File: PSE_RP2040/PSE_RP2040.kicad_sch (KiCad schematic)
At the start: 69 parts, among them IC2 SAM-M8Q-0, J1 USB_B, J2 USB_B_Micro, J3 8P8C_LED, Q1 DTC114Y, Q2 Q_PMOS_GSD, SW1 SW_Push, U1 RP2040, U2 PCF8563T, U6 PAM7Q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

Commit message: OR a diodi, connettore ext PoE
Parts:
- C2, C5: footprint (none) -> Capacitor_SMD:C_0603_1608Metric
- D1: value (none) -> D_Schottky
- D2, D3: footprint (none) -> Package_SO:SO-4_4.4x3.6mm_P2.54mm
- H1, H2, H3, H4: footprint (none) -> MountingHole:MountingHole_3mm
- IC2: footprint (none) -> PSE2021:SAM-M8Q
- J4: value (none) -> Conn_01x03; footprint (none) -> Connector_PinHeader_2.54mm:PinHeader_1x03_P2.54mm_Vertical
- R37: value (none) -> 1k; footprint (none) -> Resistor_SMD:R_0603_1608Metric
- SW2: value (none) -> SW_Push; footprint (none) -> Button_Switch_SMD:SW_SPST_EVQP0
- U5: value (none) -> W25Q16JVUXIQ; footprint (none) -> Package_SO:SOIC-8_5.275x5.275mm_P1.27mm
- Y2: footprint (none) -> Crystal:Crystal_SMD_3225-4Pin_3.2x2.5mm_HandSoldering
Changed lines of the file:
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@@
       (effects (font (size 1.27 1.27)) (justify left))
     )
-    (property "Footprint" "" (id 2) (at 105.1052 97.79 0)
+    (property "Footprint" "Capacitor_SMD:C_0603_1608Metric" (id 2) (at 105.1052 97.79 0)
       (effects (font (size 1.27 1.27)) hide)
     )
@@
       (effects (font (size 1.27 1.27)) (justify left))
     )
-    (property "Footprint" "" (id 2) (at 127.9652 97.79 0)
+    (property "Footprint" "Capacitor_SMD:C_0603_1608Metric" (id 2) (at 127.9652 97.79 0)
       (effects (font (size 1.27 1.27)) hide)
     )
@@
       (effects (font (size 1.27 1.27)) (justify left))
     )
-    (property "Footprint" "" (id 2) (at 375.92 148.59 0)
+    (property "Footprint" "PSE2021:SAM-M8Q" (id 2) (at 375.92 148.59 0)
       (effects (font (size 1.27 1.27)) (justify left) hide)
     )
@@
     (in_bom yes) (on_board yes)
     (property "Reference" "U5" (id 0) (at 345.44 50.419 0))
-    (property "Value" "" (id 1) (at 345.44 52.7304 0))
-    (property "Footprint" "" (id 2) (at 341.63 63.5 0)
+    (property "Value" "W25Q16JVUXIQ" (id 1) (at 345.44 52.7304 0))
+    (property "Footprint" "Package_SO:SOIC-8_5.275x5.275mm_P1.27mm" (id 2) (at 341.63 63.5 0)
       (effects (font (size 1.27 1.27)) hide)
     )
@@
       (effects (font (size 1.27 1.27)) (justify left))
     )
-    (property "Footprint" "" (id 2) (at 115.57 86.36 0)
+    (property "Footprint" "Crystal:Crystal_SMD_3225-4Pin_3.2x2.5mm_HandSoldering" (id 2) (at 115.57 86.36 0)
       (effects (font (size 1.27 1.27)) hide)
     )
@@
     (in_bom yes) (on_board yes)
     (property "Reference" "J4" (id 0) (at 274.32 95.25 0))
-    (property "Value" "" (id 1) (at 278.9428 91.8464 0))
-    (property "Footprint" "" (id 2) (at 276.86 97.79 0)
+    (property "Value" "Conn_01x03" (id 1) (at 278.9428 91.8464 0))
+    (property "Footprint" "Connector_PinHeader_2.54mm:PinHeader_1x03_P2.54mm_Vertical" (id 2) (at 276.86 97.79 0)
       (effects (font (size 1.27 1.27)) hide)
     )
@@
       (effects (font (size 1.27 1.27)) (justify left))
     )
-    (property "Value" "" (id 1) (at 115.57 40.6399 0)
-      (effects (font (size 1.27 1.27)) (justify left))
-    )
-    (property "Footprint" "" (id 2) (at 111.252 39.37 90)
+    (property "Value" "1k" (id 1) (at 115.57 40.6399 0)
+      (effects (font (size 1.27 1.27)) (justify left))
+    )
+    (property "Footprint" "Resistor_SMD:R_0603_1608Metric" (id 2) (at 111.252 39.37 90)
       (effects (font (size 1.27 1.27)) hide)
     )
@@
       (effects (font (size 1.27 1.27)) (justify right))
     )
-    (property "Value" "" (id 1) (at 53.34 122.2374 90)
+    (property "Value" "D_Schottky" (id 1) (at 53.34 122.2374 90)
       (effects (font (size 1.27 1.27)) (justify right))
     )
@@
     (property "Reference" "H1" (id 0) (at 24.13 271.3822 0))
     (property "Value" "MountingHole" (id 1) (at 24.13 273.9191 0))
-    (property "Footprint" "" (id 2) (at 24.13 276.86 0)
+    (property "Footprint" "MountingHole:MountingHole_3mm" (id 2) (at 24.13 276.86 0)
       (effects (font (size 1.27 1.27)) hide)
     )
@@
     (property "Reference" "D3" (id 0) (at 211.4558 213.3433 90))
     (property "Value" "D_Bridge_+-AA" (id 1) (at 211.4558 215.8802 90))
-    (property "Footprint" "" (id 2) (at 198.12 217.17 0)
+    (property "Footprint" "Package_SO:SO-4_4.4x3.6mm_P2.54mm" (id 2) (at 198.12 217.17 0)
       (effects (font (size 1.27 1.27)) hide)
     )
@@
       (effects (font (size 1.27 1.27)) (justify left))
     )
-    (property "Value" "" (id 1) (at 116.84 50.7999 90)
-      (effects (font (size 1.27 1.27)) (justify left))
-    )
-    (property "Footprint" "" (id 2) (at 118.11 49.53 0)
+    (property "Value" "SW_Push" (id 1) (at 116.84 50.7999 90)
+      (effects (font (size 1.27 1.27)) (justify left))
+    )
+    (property "Footprint" "Button_Switch_SMD:SW_SPST_EVQP0" (id 2) (at 118.11 49.53 0)
       (effects (font (size 1.27 1.27)) hide)
     )
@@
     (property "Reference" "D2" (id 0) (at 211.4558 189.7211 90))
     (property "Value" "D_Bridge_+-AA" (id 1) (at 211.4558 192.258 90))
-    (property "Footprint" "" (id 2) (at 198.12 194.31 0)
+    (property "Footprint" "Package_SO:SO-4_4.4x3.6mm_P2.54mm" (id 2) (at 198.12 194.31 0)
       (effects (font (size 1.27 1.27)) hide)
     )
@@
       (effects (font (size 1.27 1.27)) hide)
     )
-    (property "Value" "" (id 1) (at 113.03 59.69 0))
+    (property "Value" "GND" (id 1) (at 113.03 59.69 0))
     (property "Footprint" "" (id 2) (at 113.03 54.61 0)
       (effects (font (size 1.27 1.27)) hide)
@@
     (property "Reference" "H4" (id 0) (at 80.01 271.3822 0))
     (property "Value" "MountingHole" (id 1) (at 80.01 273.9191 0))
-    (property "Footprint" "" (id 2) (at 80.01 276.86 0)
+    (property "Footprint" "MountingHole:MountingHole_3mm" (id 2) (at 80.01 276.86 0)
       (effects (font (size 1.27 1.27)) hide)
     )
@@
     (property "Reference" "H3" (id 0) (at 60.96 271.3822 0))
     (property "Value" "MountingHole" (id 1) (at 60.96 273.9191 0))
-    (property "Footprint" "" (id 2) (at 60.96 276.86 0)
+    (property "Footprint" "MountingHole:MountingHole_3mm" (id 2) (at 60.96 276.86 0)
       (effects (font (size 1.27 1.27)) hide)
     )
@@
     (property "Reference" "H2" (id 0) (at 41.91 271.3822 0))
     (property "Value" "MountingHole" (id 1) (at 41.91 273.9191 0))
-    (property "Footprint" "" (id 2) (at 41.91 276.86 0)
+    (property "Footprint" "MountingHole:MountingHole_3mm" (id 2) (at 41.91 276.86 0)
       (effects (font (size 1.27 1.27)) hide)
     )
@@
       (reference "#FLG0107") (unit 1) (value "PWR_FLAG") (footprint "")
     )
+    (path "/cfa038c0-a49f-45bf-b6e3-72692695ea2c/48e056eb-b81b-4424-9906-730b85dc5ede"
+      (reference "#PWR01") (unit 1) (value "GND") (footprint "")
+    )
+    (path "/cfa038c0-a49f-45bf-b6e3-72692695ea2c/7345524d-162d-49f9-b059-7d50670e840d"
+      (reference "#PWR02") (unit 1) (value "GND") (footprint "")
+    )
+    (path "/cfa038c0-a49f-45bf-b6e3-72692695ea2c/f2069746-1acd-473c-afc9-f4cddcfc0d27"
+      (reference "#PWR03") (unit 1) (value "+5V") (footprint "")
+    )
     (path "/00000000-0000-0000-0000-0000622de161"
       (reference "#PWR0101") (unit 1) (value "GND") (footprint "")
@@
       (reference "D6") (unit 1) (value "D_Schottky") (footprint "Diode_SMD:D_SMA")
     )
+    (path "/cfa038c0-a49f-45bf-b6e3-72692695ea2c/a61d4b07-497e-4038-b25b-f79b916f4673"
+      (reference "D7") (unit 1) (value "1.5KExxA") (footprint "Diode_THT:D_DO-201AE_P15.24mm_Horizontal")
+    )
+    (path "/cfa038c0-a49f-45bf-b6e3-72692695ea2c/48d1f8a7-bc8d-42c0-99ef-de81f70d61e6"
+      (reference "D8") (unit 1) (value "D") (footprint "")
+    )
+    (path "/cfa038c0-a49f-45bf-b6e3-72692695ea2c/61cb9ba8-b974-4c1c-9a84-fd9c3e022760"
+      (reference "D9") (unit 1) (value "D_Schottky") (footprint "Diode_SMD:D_SMA")
+    )
     (path "/74e5bcde-a2f3-4e4c-9540-20adf9b3b91b"
       (reference "E1") (unit 1) (value "SparkGap") (footprint "")
     )
+    (path "/cfa038c0-a49f-45bf-b6e3-72692695ea2c/97ab722b-fd8d-4740-9e40-4c3e59877c7d"
+      (reference "F1") (unit 1) (value "Polyfuse_Small") (footprint "")
+    )
     (path "/6ccbb867-9e07-437e-8116-e1e188734541"
       (reference "H1") (unit 1) (value "MountingHole") (footprint "MountingHole:MountingHole_3mm")
@@
       (reference "J4") (unit 1) (value "Conn_01x03") (footprint "Connector_PinHeader_2.54mm:PinHeader_1x03_P2.54mm_Vertical")
     )
+    (path "/cfa038c0-a49f-45bf-b6e3-72692695ea2c/f580e39d-850d-43de-bd68-8978c3e2ed53"
+      (reference "J5") (unit 1) (value "Barrel_Jack") (footprint "")
+    )
     (path "/cfa038c0-a49f-45bf-b6e3-72692695ea2c/3e85cecd-b5b0-4747-993b-fc187c4ec79a"

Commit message: correzioni schema
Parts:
- removed Q1: DTC114Y, symbol Transistor_BJT:DTC114Y
- C1: value 1F -> (none); footprint Capacitor_SMD:C_0805_2012Metric -> (none)
- C12, C14, C18: footprint (none) -> Capacitor_SMD:C_0603_1608Metric
- D4: footprint (none) -> LED_SMD:LED_0603_1608Metric
- TP11: value VCC -> (none)
- U5: value W25Q16JVUXIQ -> (none)
- Y1: value Crystal_GND3 -> (none); footprint Crystal:Crystal_AT310_D3.0mm_L10.0mm_Horizontal_1EP_style1 -> (none)
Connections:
- net GPS_EN: now also Q2.1 (G), R27.1
- net VCC renamed VCC_GPS
- no-connect marks 15 -> 13
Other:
- note added: "pullup interno mcu"

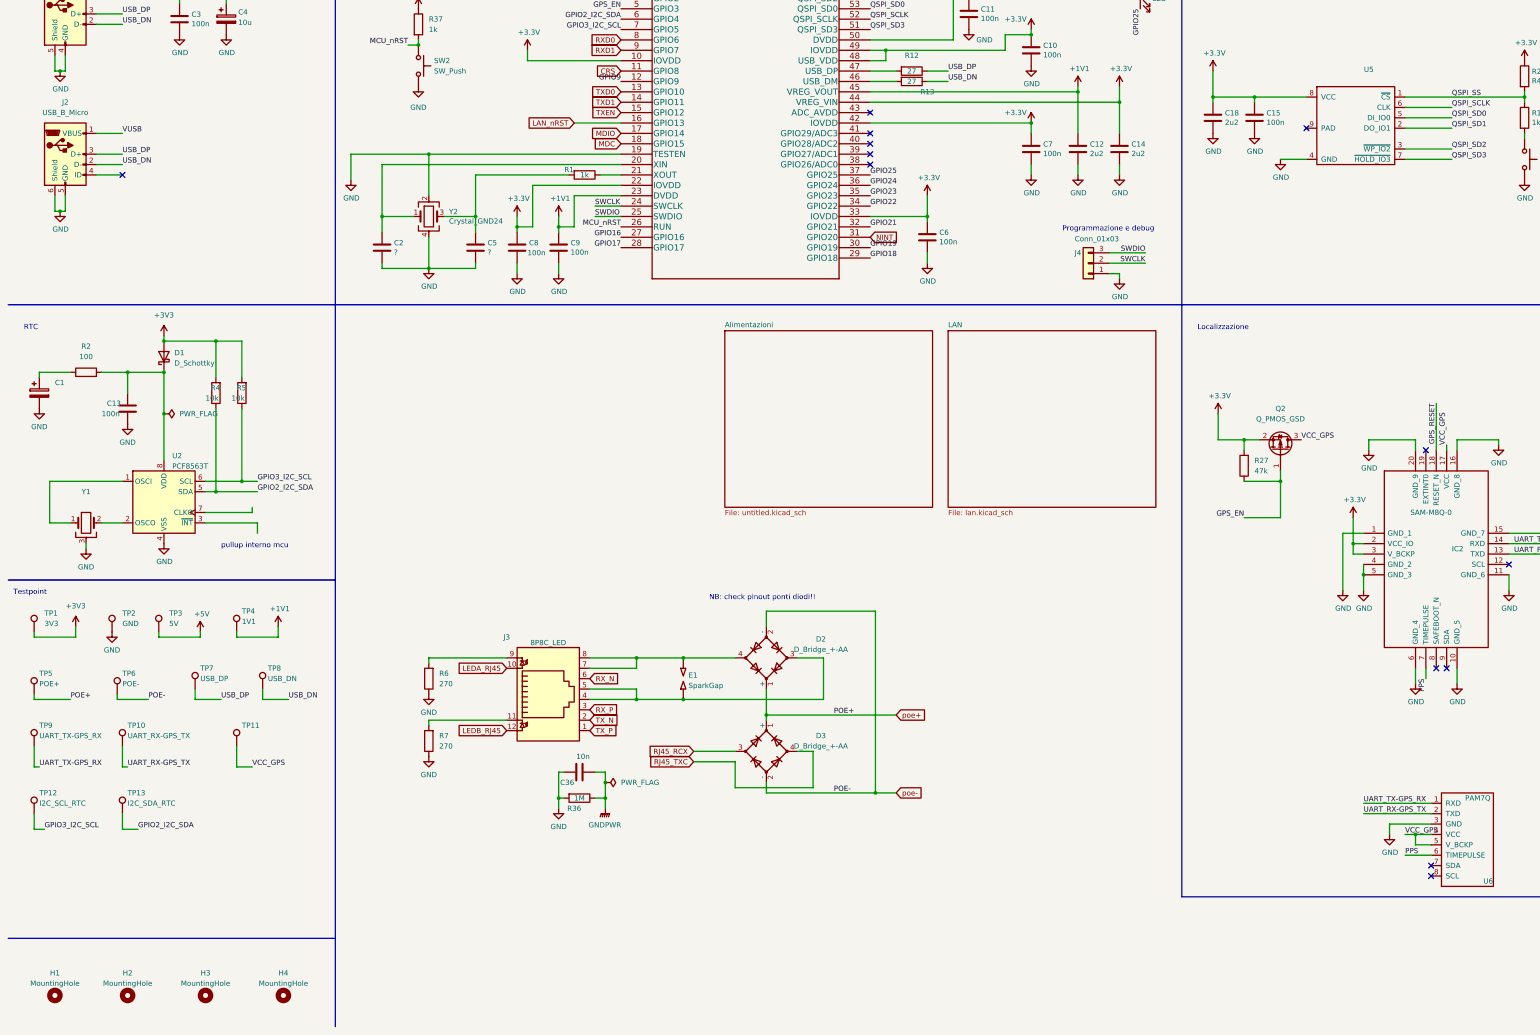
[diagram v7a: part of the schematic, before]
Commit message: footprint, assegnamento
etichette (label)
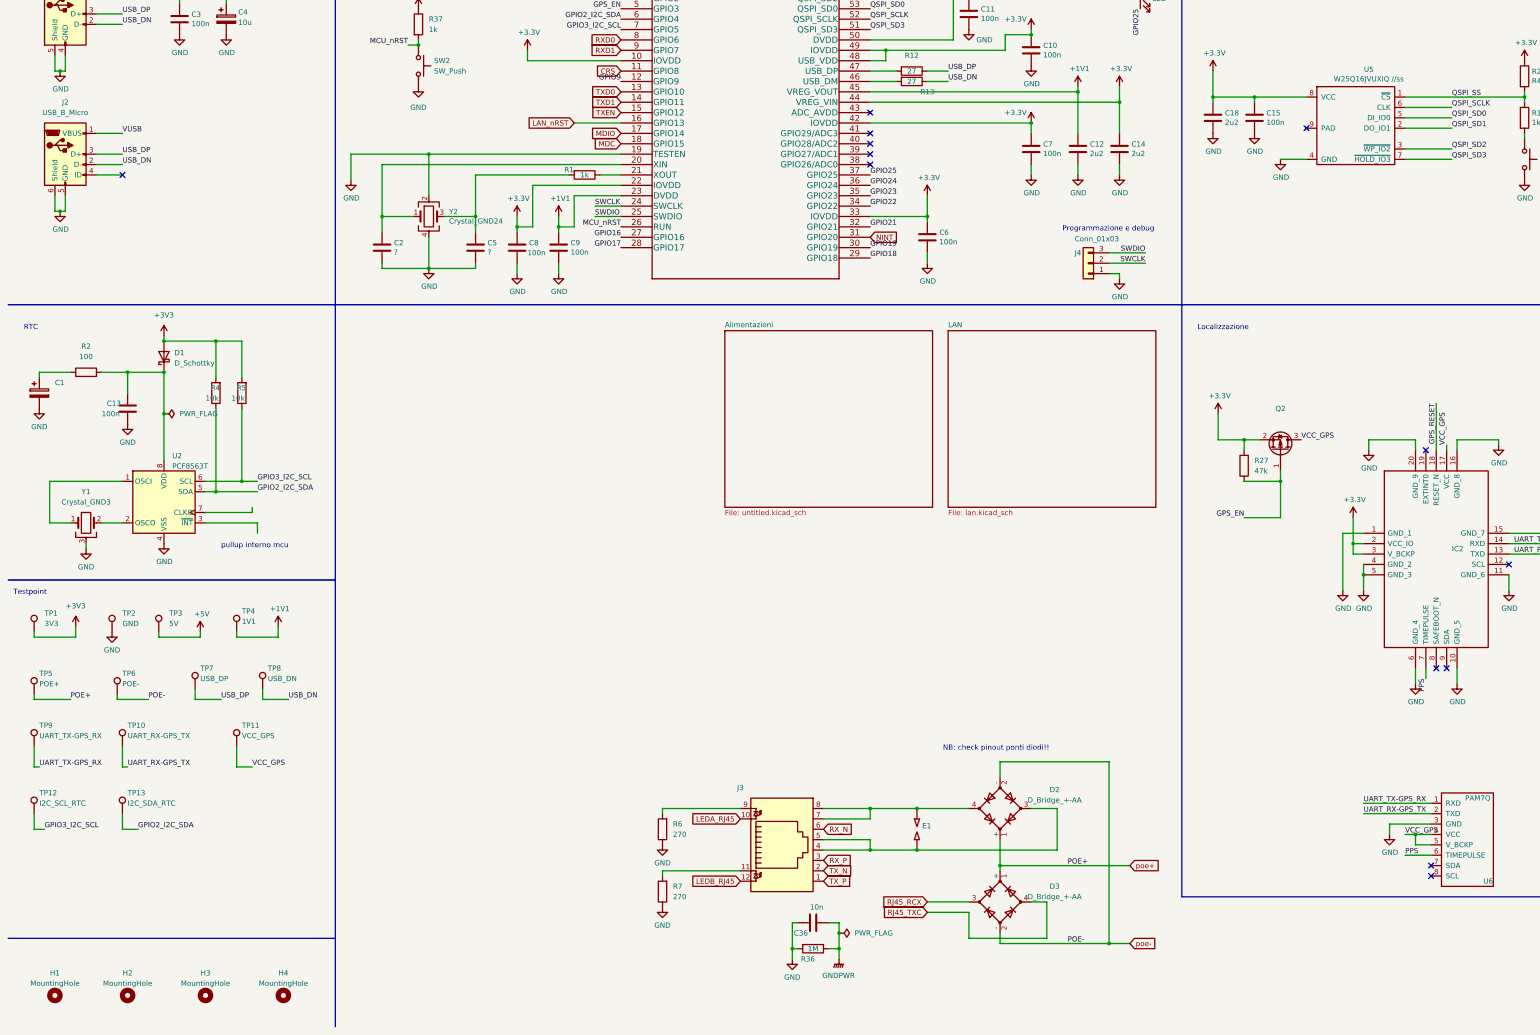
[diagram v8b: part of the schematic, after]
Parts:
- E1: value SparkGap -> (none)
- IC2: value SAM-M8Q-0 -> (none); footprint PSE2021:SAM-M8Q -> (none)
- J3: value 8P8C_LED -> (none)
- Q2: value Q_PMOS_GSD -> (none)
- TP11: value (none) -> VCC_GPS
- U5: value (none) -> W25Q16JVUXIQ //ss
- Y1: value (none) -> Crystal_GND3; footprint (none) -> Crystal:Crystal_AT310_D3.0mm_L10.0mm_Horizontal_1EP_style1
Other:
- moved on the sheet: C36, D2, D3, E1, J3, R36, R6, R7
